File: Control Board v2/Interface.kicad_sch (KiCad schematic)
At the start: 0 parts

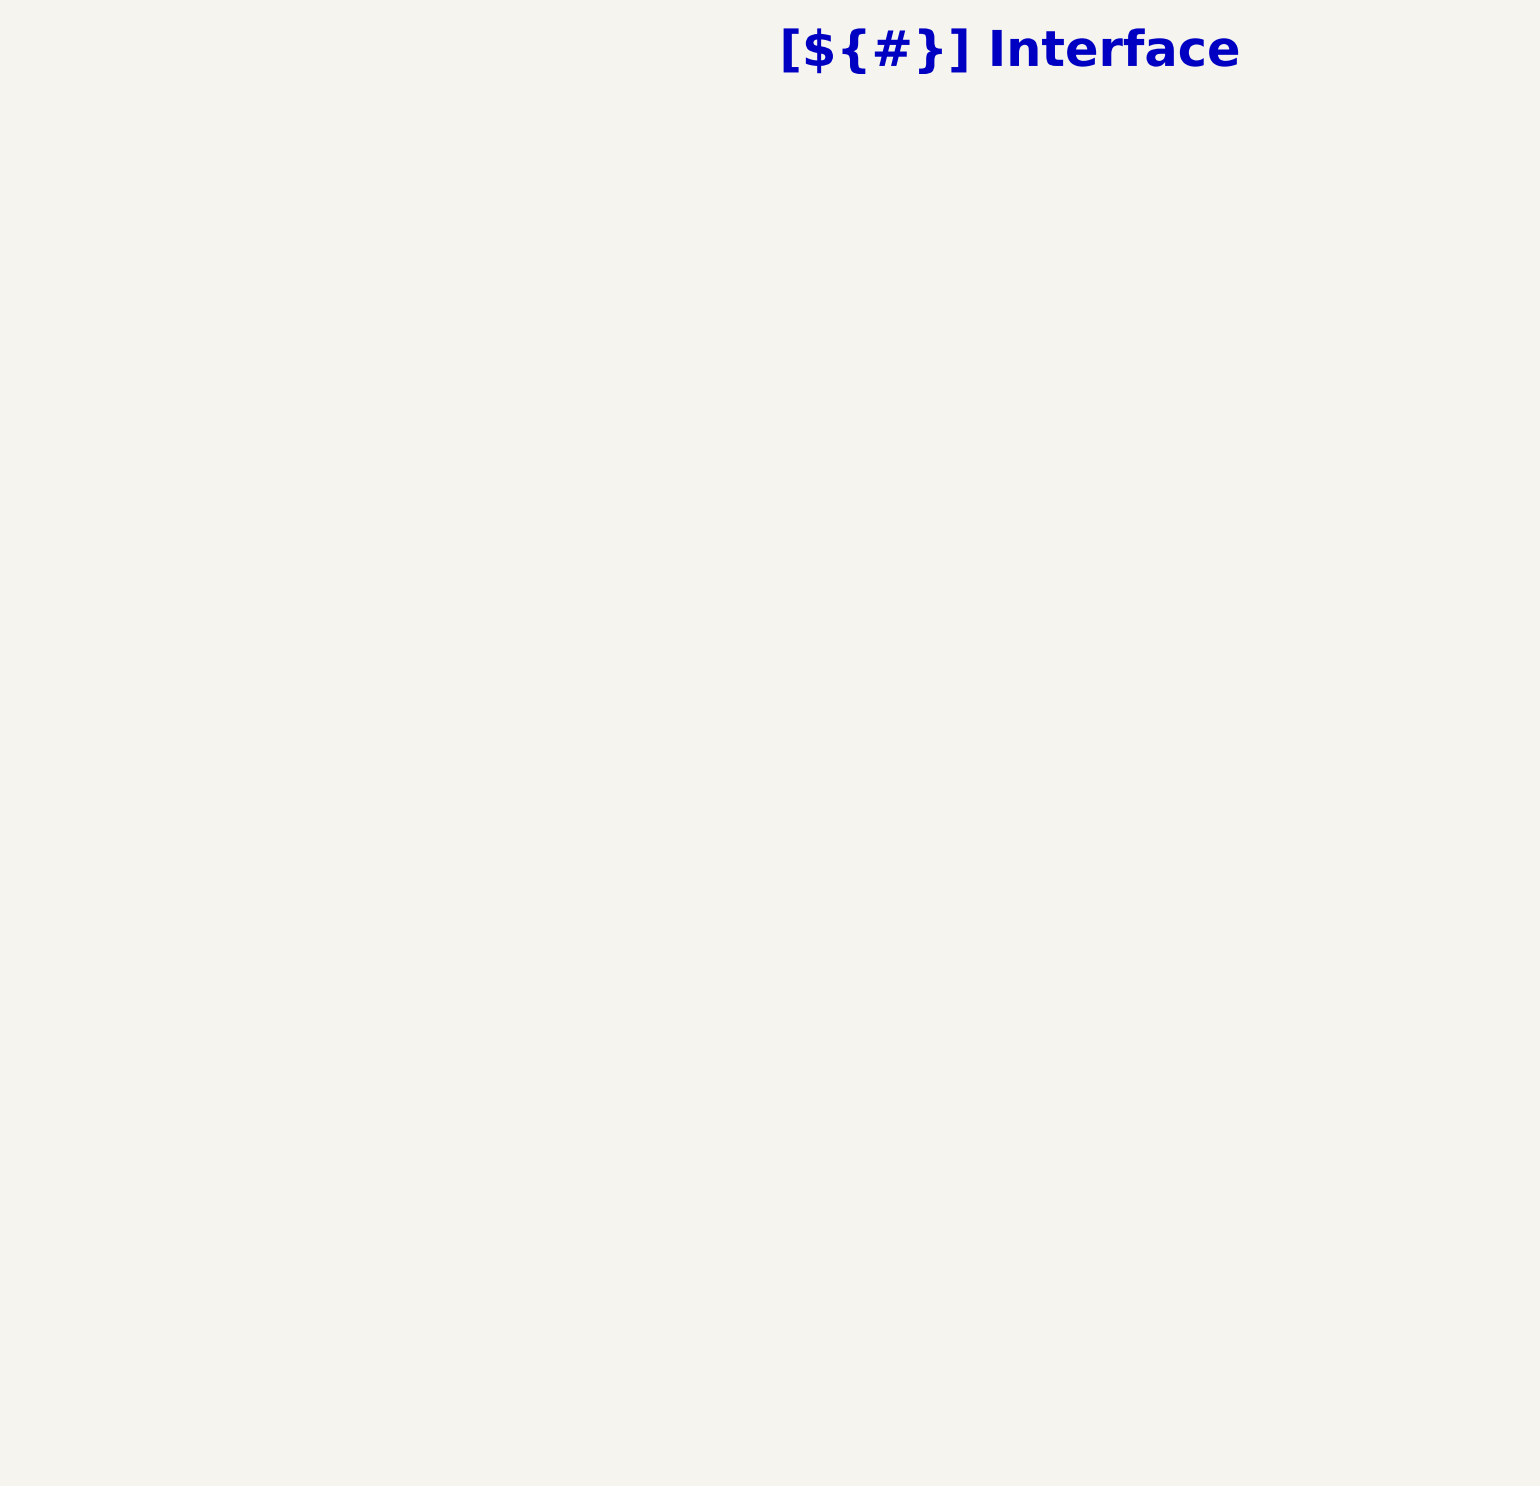
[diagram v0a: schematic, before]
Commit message: draft microcontroller and interface circuits, still need to finish interfaces
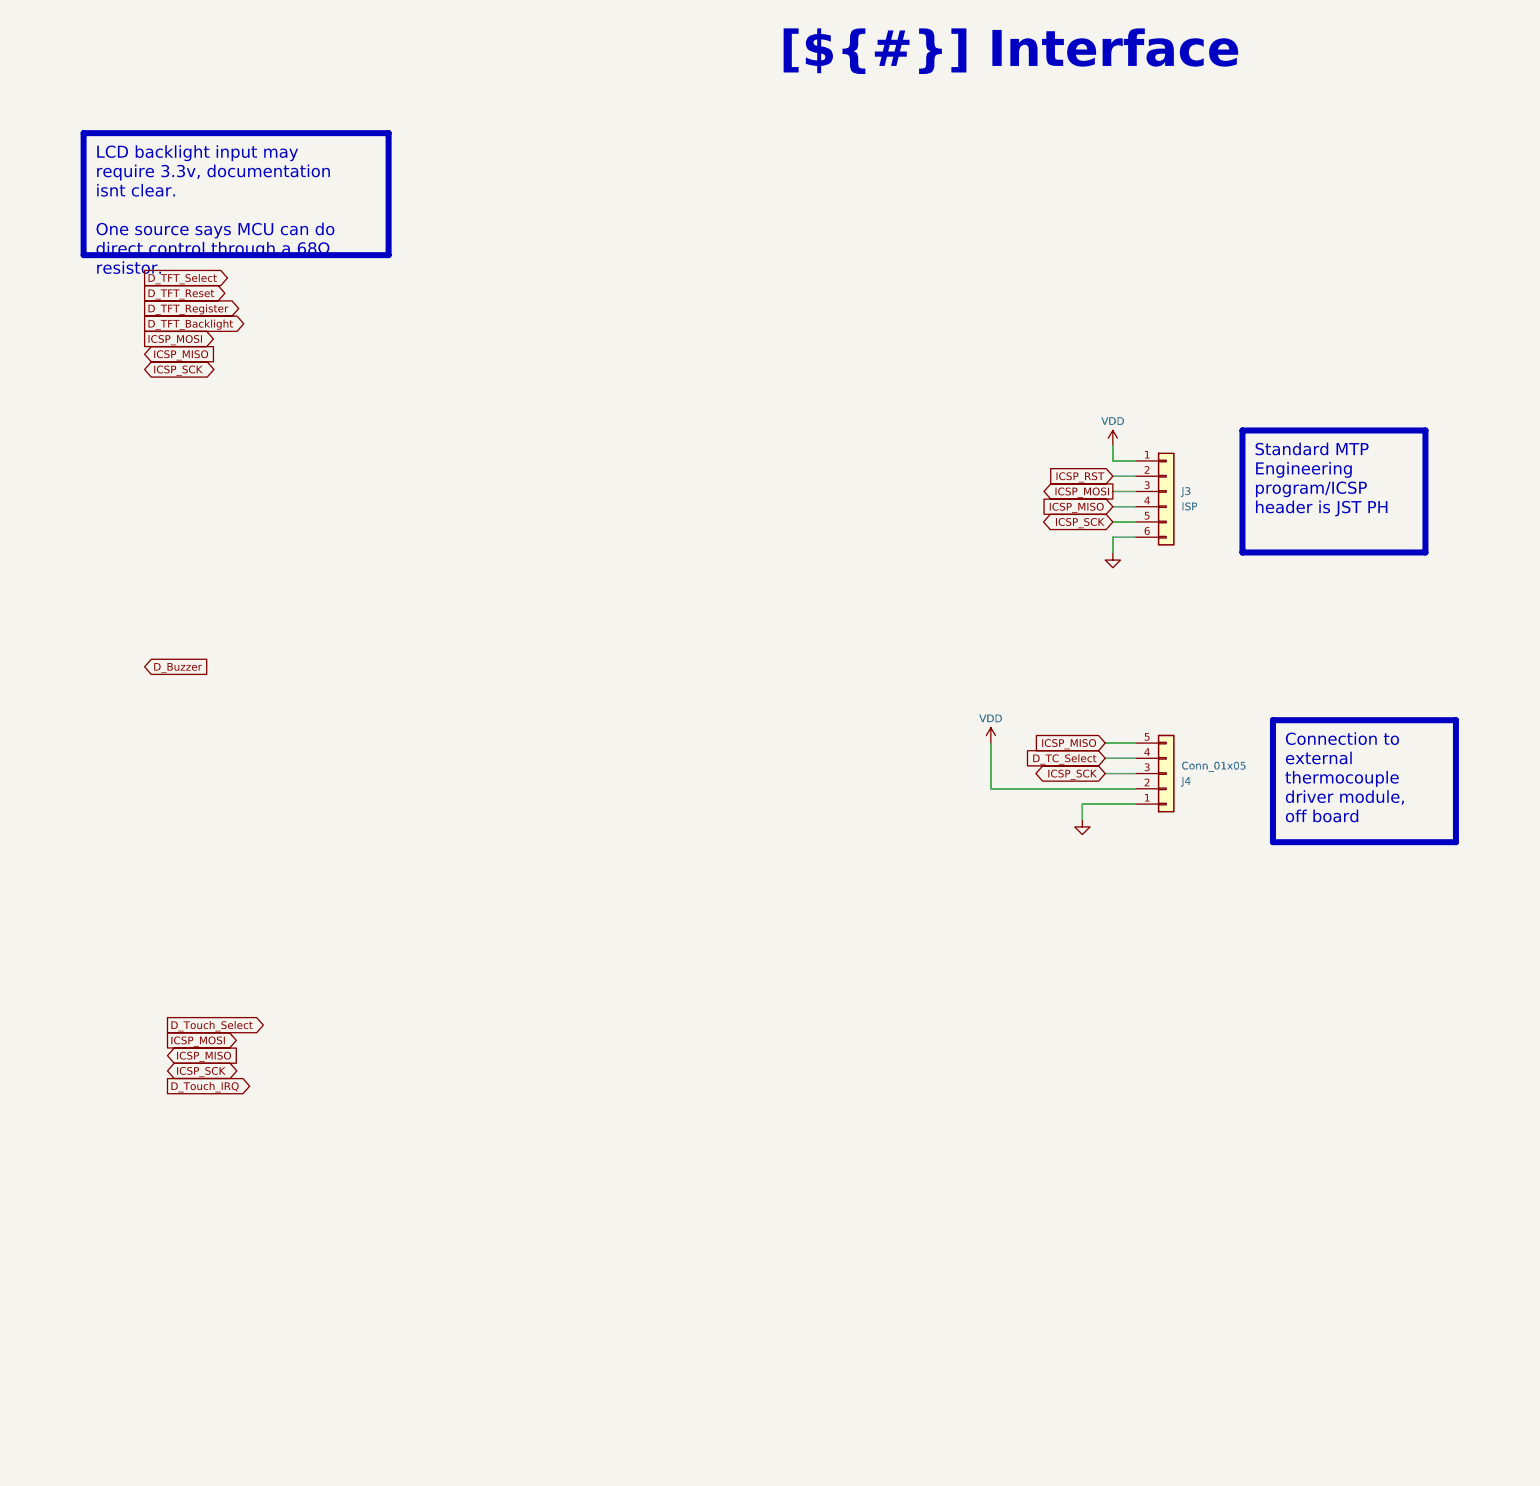
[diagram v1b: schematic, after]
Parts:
- added J3: ISP, Connector_JST:JST_PH_B6B-PH-K_1x06_P2.00mm_Vertical, symbol Connector_Generic:Conn_01x06
- added J4: Conn_01x05, Connector_JST:JST_XH_B5B-XH-A_1x05_P2.50mm_Vertical, symbol Connector_Generic:Conn_01x05
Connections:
- new net D_TC_Select: J4.4 (Pin_4)
- new net GND: J3.6 (Pin_6), J4.1 (Pin_1)
- new net ICSP_MISO: J3.4 (Pin_4), J4.5 (Pin_5)
- new net ICSP_MOSI: J3.3 (Pin_3)
- new net ICSP_RST: J3.2 (Pin_2)
- new net ICSP_SCK: J3.5 (Pin_5), J4.3 (Pin_3)
- new net VDD: J3.1 (Pin_1), J4.2 (Pin_2)

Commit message: work on PCB layout
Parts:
- added BZ1: CMI-0955-05TH, Buzzer_Beeper:MagneticBuzzer_PUI_AT-0927-TT-6-R, symbol Device:Buzzer
- added J5: Conn_01x14, Connector_PinSocket_2.54mm:PinSocket_1x14_P2.54mm_Vertical, symbol Connector_Generic:Conn_01x14
- added JP1, JP2: Jumper_2_Open, Jumper:SolderJumper-2_P1.3mm_Open_RoundedPad1.0x1.5mm, symbol Jumper:Jumper_2_Open
- added Q1: SQ2315CES-T1_GE3, Package_TO_SOT_SMD:SOT-23_Handsoldering, symbol Simulation_SPICE:PMOS
- added Q2: BSS127 H6327, Package_TO_SOT_SMD:SOT-23_Handsoldering, symbol Simulation_SPICE:NMOS
- added R6: 330, Resistor_SMD:R_0402_1005Metric, symbol Device:R_Small_US
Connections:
- net D_Buzzer: now also Q2.2 (G)
- net D_TFT_Backlight: now also Q1.2 (G)
- net D_TFT_Register: now also J5.10 (Pin_10)
- net D_TFT_Reset: now also J5.11 (Pin_11)
- net D_TFT_Select: now also J5.12 (Pin_12)
- net D_Touch_IRQ: now also J5.1 (Pin_1)
- net D_Touch_Select: now also J5.4 (Pin_4)
- net GND: now also J5.13 (Pin_13), Q2.3 (S)
- net ICSP_MISO: now also J5.2 (Pin_2), J5.6 (Pin_6)
- net ICSP_MOSI: now also J5.3 (Pin_3), J5.9 (Pin_9)
- net ICSP_SCK: now also J5.5 (Pin_5), J5.8 (Pin_8)
- net VDD: now also J5.14 (Pin_14), JP2.2 (B), R6.2
- new net VDD_BL: J5.7 (Pin_7), JP1.2 (B)
- new net VDD_BL_FET: JP1.1 (A), Q1.3 (S)
- new net VDD_BL_SUP: JP2.1 (A), Q1.1 (D)
- new net VDD_BUZZ: BZ1.1 (+), R6.1
- new net VSS_BUZZ: BZ1.2 (-), Q2.1 (D)
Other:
- note added: "BSS127 H6327 Datasheet"
- note added: "CMI-0955-05TH Datasheet"
- note added: "SQ2315CES-T1_GE3 Datasheet"
